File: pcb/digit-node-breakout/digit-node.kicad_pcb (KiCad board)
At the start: 2 copper layers, 20 parts, among them J1 Conn_01x09_Male, J2 STM32_SWD, Q1 PZT2222A, Q2 PZT2222A, U1 STM32F030F4Px

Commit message: More digit PCB cleanup
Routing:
- net Net-(J1-Pad3): track 60.8 -> 63.8 mm

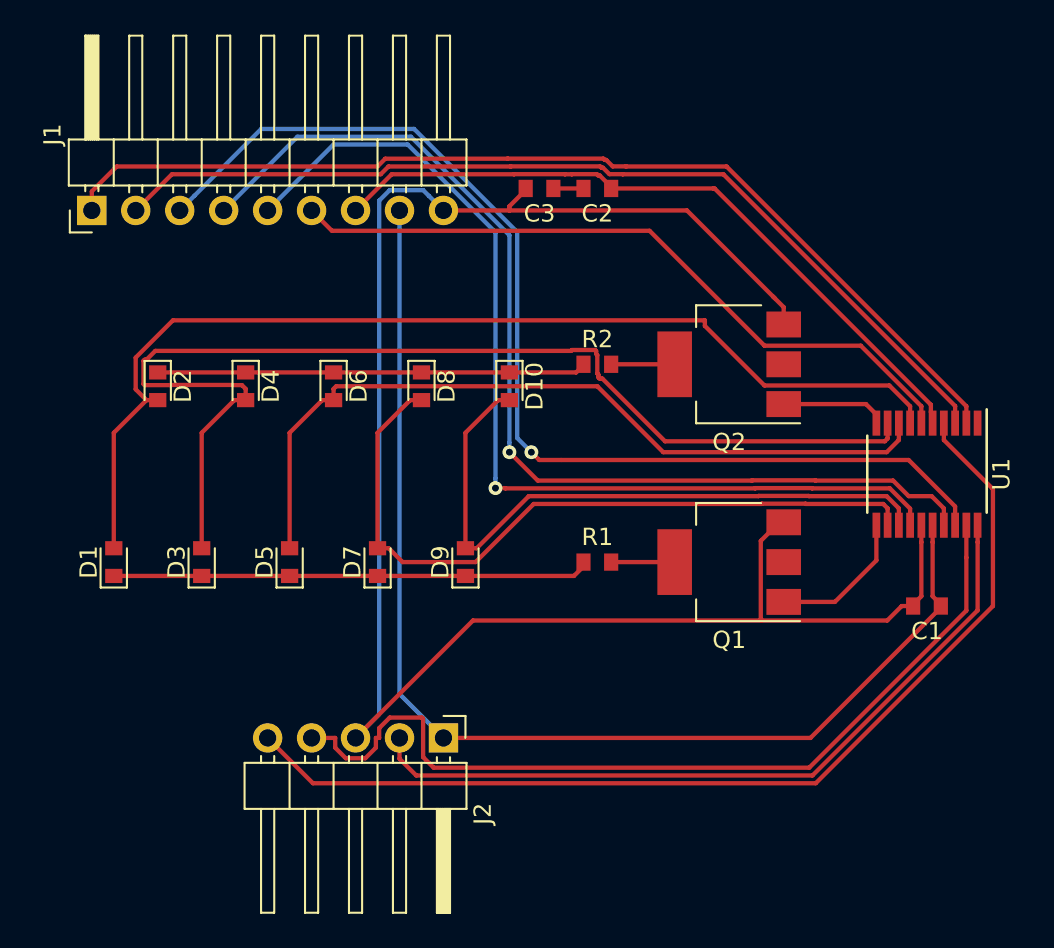
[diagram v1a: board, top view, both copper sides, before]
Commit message: Digit PCB is now 100% via-free!
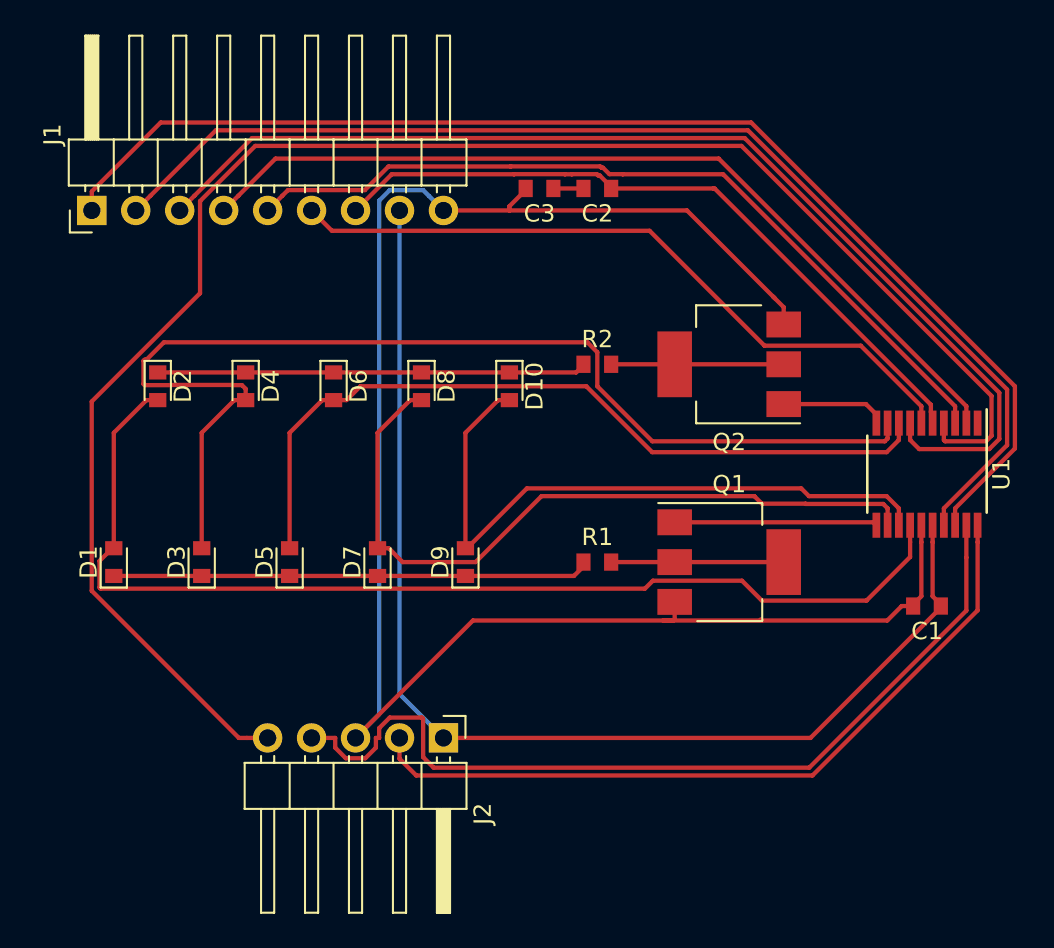
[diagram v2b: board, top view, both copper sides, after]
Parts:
- turned Q1 to 0 degrees
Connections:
- U1 pad 14: Net-(J1-Pad5) -> /led_matrix/led_01
- U1 pad 17: Net-(J1-Pad4) -> Net-(J1-Pad2)
- U1 pad 18: Net-(J1-Pad3) -> Net-(J1-Pad1)
- U1 pad 2: Net-(J1-Pad1) -> Net-(J1-Pad4)
- U1 pad 3: Net-(J1-Pad2) -> Net-(J1-Pad5)
- U1 pad 7: /led_matrix/led_01 -> Net-(J1-Pad3)
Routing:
- net Net-(J2-Pad5): track 59.0 -> 98.0 mm
- net Net-(J1-Pad2): track 55.1 -> 67.8 mm
- net Net-(J1-Pad1): track 59.3 -> 71.9 mm
- net Net-(J1-Pad5): track 57.0 -> 47.5 mm, vias 1 -> 0
- net Net-(J1-Pad4): track 60.6 -> 51.1 mm, vias 1 -> 0
- net Net-(Q2-Pad2): track 3.72 -> 10.0 mm
- net Net-(Q1-Pad2): track 3.72 -> 10.0 mm
- net GND: track 107.5 -> 102.9 mm
- net Net-(Q1-Pad1): track 8.38 -> 11.7 mm
- net /led_matrix/led_01: track 61.6 -> 63.1 mm
- net /led_matrix/led_23: track 65.2 -> 65.9 mm
- net Net-(J1-Pad3): track 63.8 -> 64.4 mm, vias 1 -> 0

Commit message: Moved the pin headers closer to each other
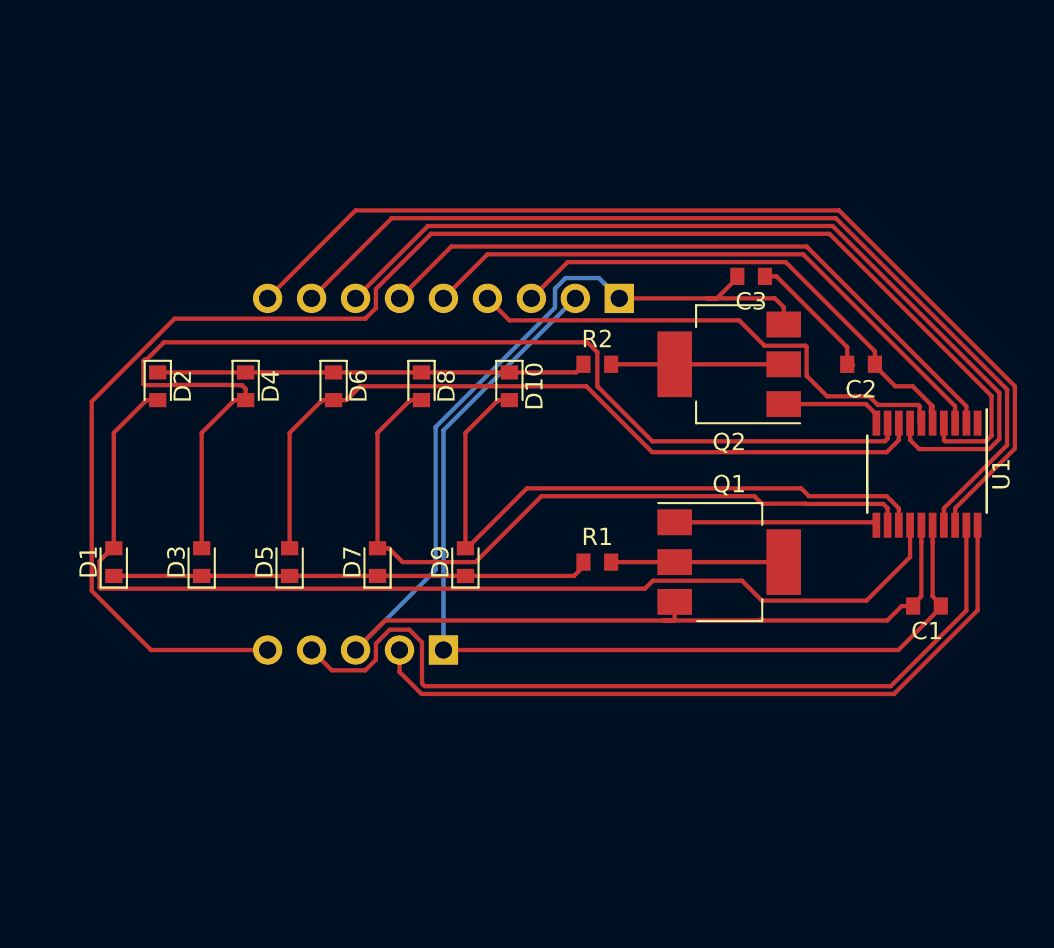
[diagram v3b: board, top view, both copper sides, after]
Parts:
- J1: footprint Connector_PinHeader_2.54mm:PinHeader_1x09_P2.54mm_Horizontal -> Connector_PinHeader_2.54mm:PinHeader_1x09_P2.54mm_Vertical; moved to B.Cu
- J2: footprint Connector_PinHeader_2.54mm:PinHeader_1x05_P2.54mm_Horizontal -> Connector_PinHeader_2.54mm:PinHeader_1x05_P2.54mm_Vertical; moved to B.Cu
- moved J1 30.9 mm to (130.8, 77.5)
- moved C2 18.3 mm to (144.8, 81.3)
- moved C3 13.2 mm to (138.4, 76.2)
- moved J2 5.08 mm to (120.7, 97.8), turned to 90 degrees
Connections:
- J1 pad 1: Net-(J1-Pad1) -> GND
- J1 pad 2: Net-(J1-Pad2) -> VDD
- J1 pad 3: Net-(J1-Pad3) -> VDDA
- J1 pad 7: VDDA -> Net-(J1-Pad7)
- J1 pad 8: VDD -> Net-(J1-Pad8)
- J1 pad 9: GND -> Net-(J1-Pad9)
- U1 pad 17: Net-(J1-Pad2) -> Net-(J1-Pad8)
- U1 pad 18: Net-(J1-Pad1) -> Net-(J1-Pad9)
- U1 pad 2: Net-(J1-Pad4) -> Net-(J1-Pad6)
- U1 pad 6: Net-(J1-Pad6) -> Net-(J1-Pad4)
- U1 pad 7: Net-(J1-Pad3) -> Net-(J1-Pad7)
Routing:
- net Net-(J1-Pad1): track 71.9 -> 0.00 mm
- net Net-(J1-Pad2): track 67.8 -> 0.00 mm
- net Net-(J1-Pad3): track 64.4 -> 0.00 mm
- net Net-(J1-Pad9): track 0.00 -> 59.0 mm
- net Net-(J1-Pad8): track 0.00 -> 55.6 mm
- net Net-(J1-Pad7): track 0.00 -> 52.2 mm
- net Net-(J1-Pad4): track 51.1 -> 29.6 mm
- net GND: track 102.9 -> 83.1 mm
- net Net-(J1-Pad5): track 47.5 -> 35.2 mm
- net VDDA: track 40.8 -> 30.1 mm
- net VDD: track 68.3 -> 58.2 mm
- net Net-(J2-Pad5): track 98.0 -> 89.2 mm
- net Net-(C2-Pad2): track 1.74 -> 7.52 mm
- net Net-(J2-Pad4): track 51.5 -> 49.3 mm
- net Net-(J1-Pad6): track 40.9 -> 38.8 mm
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
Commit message: Even more compact!
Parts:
- moved C1 3.81 mm to (144.8, 95.2)
- moved U1 2.54 mm to (146.1, 87.6)
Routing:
- net VDD: track 58.2 -> 54.5 mm
- net GND: track 83.1 -> 79.7 mm
- net Net-(J1-Pad4): track 29.6 -> 26.7 mm
- net Net-(J2-Pad4): track 49.3 -> 46.4 mm
- net /led_matrix/led_01: track 63.1 -> 60.3 mm
- net VDDA: track 30.1 -> 27.4 mm
- net Net-(Q2-Pad1): track 6.10 -> 3.56 mm
- net Net-(Q1-Pad1): track 11.7 -> 9.19 mm
- net /led_matrix/led_89: track 37.9 -> 35.4 mm
- net /led_matrix/led_67: track 42.6 -> 40.1 mm
- net /led_matrix/led_45: track 45.8 -> 43.6 mm
- net /led_matrix/led_23: track 65.9 -> 63.9 mm
- net Net-(J2-Pad2): track 42.1 -> 41.0 mm
- net Net-(J1-Pad5): track 35.2 -> 34.2 mm
- net Net-(J1-Pad6): track 38.8 -> 37.8 mm
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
